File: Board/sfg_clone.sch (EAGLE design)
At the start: 121 parts, among them IC1 27C512AP, IC2 74LS04D, IC3 EPM7160-T100, IC4 YM2151, IC5 YM3012, IC6 LM4556N, IC7 LM4556N, IC8 LM4558N, IC9 TLP552, Q1 4mHz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

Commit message: Board updated to version 1.1
Board updated to version 1.1
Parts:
- added C3: 47pF, rcl:C-EUC0805
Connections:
- net GND: now also C3.2
- net N$8: now also C3.1
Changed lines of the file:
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@@
 <?xml version="1.0" encoding="utf-8"?>
 <!DOCTYPE eagle SYSTEM "eagle.dtd">
-<eagle version="6.5.0">
+<eagle version="7.5.0">
 <drawing>
 <settings>
@@
 <part name="SUPPLY5" library="supply2" deviceset="+5V" device=""/>
 <part name="GND4" library="supply1" deviceset="GND" device=""/>
+<part name="C3" library="rcl" deviceset="C-EU" device="C0805" value="47pF"/>
 </parts>
 <sheets>
@@
 <instance part="C13" gate="G$1" x="264.16" y="7.62" rot="R270"/>
 <instance part="SUPPLY17" gate="+5V" x="256.54" y="30.48"/>
-<instance part="GND11" gate="1" x="256.54" y="-7.62"/>
+<instance part="GND11" gate="1" x="256.54" y="-10.16"/>
 <instance part="IC2" gate="C" x="35.56" y="78.74"/>
 <instance part="R24" gate="G$1" x="215.9" y="111.76" rot="R180"/>
@@
 <instance part="SUPPLY5" gate="+5V" x="25.4" y="134.62"/>
 <instance part="GND4" gate="1" x="25.4" y="121.92"/>
+<instance part="C3" gate="G$1" x="205.74" y="-5.08" rot="R90"/>
 </instances>
 <busses>
@@
 <junction x="256.54" y="0"/>
 <pinref part="C27" gate="G$1" pin="2"/>
+<wire x1="256.54" y1="-5.08" x2="256.54" y2="-7.62" width="0.1524" layer="91"/>
 <wire x1="276.86" y1="5.08" x2="276.86" y2="0" width="0.1524" layer="91"/>
 <wire x1="276.86" y1="0" x2="256.54" y2="0" width="0.1524" layer="91"/>
+<pinref part="C3" gate="G$1" pin="2"/>
+<wire x1="256.54" y1="-5.08" x2="210.82" y2="-5.08" width="0.1524" layer="91"/>
+<junction x="256.54" y="-5.08"/>
 </segment>
 <segment>
@@
 <wire x1="185.42" y1="5.08" x2="185.42" y2="17.78" width="0.1524" layer="91"/>
 <junction x="185.42" y="17.78"/>
-</segment>
-</net>
+<wire x1="185.42" y1="5.08" x2="185.42" y2="-5.08" width="0.1524" layer="91"/>
+<junction x="185.42" y="5.08"/>
+<pinref part="C3" gate="G$1" pin="1"/>
+<wire x1="185.42" y1="-5.08" x2="203.2" y2="-5.08" width="0.1524" layer="91"/>
+</segment>
+</net>

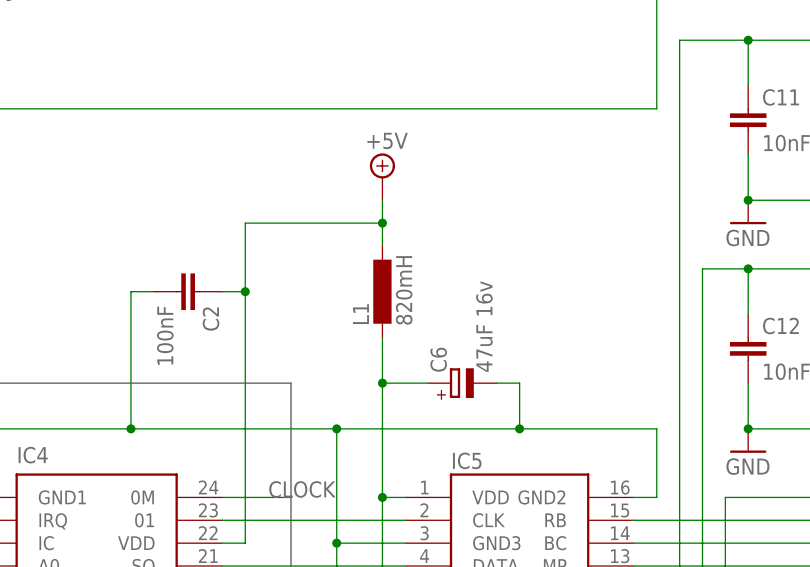
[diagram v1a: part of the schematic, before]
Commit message: Updated 21.01.2021
Fixed schematics and partslist (the value of the coil was incorrectly
specified)
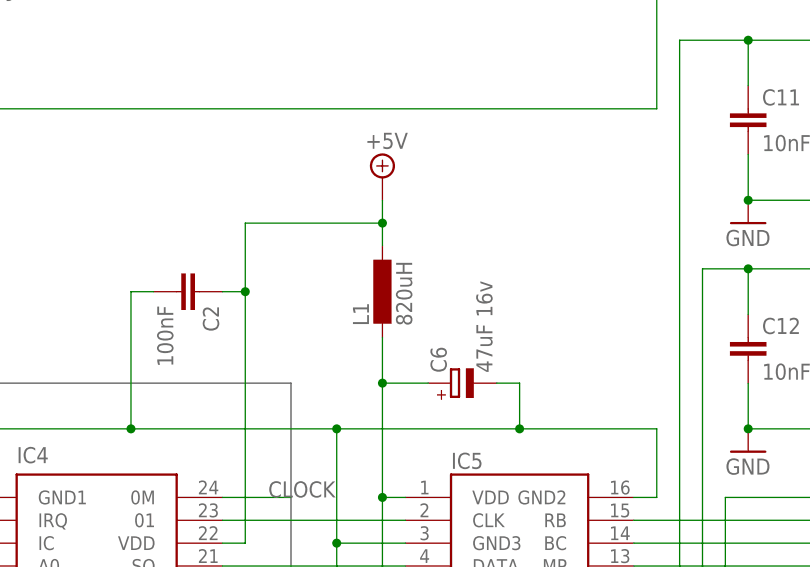
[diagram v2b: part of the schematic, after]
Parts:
- L1: value 820mH -> 820uH
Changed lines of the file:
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@@
 <part name="R22" library="resistor" deviceset="R-EU_" device="R0805" value="330"/>
 <part name="GND5" library="supply1" deviceset="GND" device=""/>
-<part name="L1" library="rcl" deviceset="L-EU" device="6000-XXX-RC" value="820mH"/>
+<part name="L1" library="rcl" deviceset="L-EU" device="6000-XXX-RC" value="820uH"/>
 <part name="C6" library="rcl" deviceset="CPOL-EU" device="SMCC" value="47uF 16v"/>
 <part name="C4" library="rcl" deviceset="C-EU" device="C0805" value="100nF"/>
